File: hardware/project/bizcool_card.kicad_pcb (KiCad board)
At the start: 4 copper layers, 85.6 x 53.9 mm, 147 parts, among them J1 XL-1005SURC, J2 Conn_01x03, SW1 SW_Push, SW2 SW_Push, U1 PRTR5V0U2X, U2 ME6211C33M5G, U3 ESP32-C3FN4, U4 W25Q128JVS

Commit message: fix: LCSC component references
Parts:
- U2: value ME6211C33M5G -> AMS1117-3.3
- U4: value W25Q128JVS -> W25Q128JVSIQ
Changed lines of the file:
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@@
     (descr "Resistor SMD 0402 (1005 Metric), square (rectangular) end terminal, IPC_7351 nominal, (Body size source: IPC-SM-782 page 72, https://www.pcb-3d.com/wordpress/wp-content/uploads/ipc-sm-782a_amendment_1_and_2.pdf), generated with kicad-footprint-generator")
     (tags "resistor")
-    (property "LCSC Part" "C965790")
+    (property "LCSC Part" "C60490")
     (property "Sheetfile" "bizcool_card.kicad_sch")
     (property "Sheetname" "")
@@
     (descr "Capacitor SMD 0402 (1005 Metric), square (rectangular) end terminal, IPC_7351 nominal, (Body size source: IPC-SM-782 page 76, https://www.pcb-3d.com/wordpress/wp-content/uploads/ipc-sm-782a_amendment_1_and_2.pdf), generated with kicad-footprint-generator")
     (tags "capacitor")
+    (property "LCSC Part" "C60133")
     (property "Sheetfile" "bizcool_card.kicad_sch")
     (property "Sheetname" "")
@@
     (descr "Miniature Crystal Clock Oscillator EuroQuartz XO32 series, http://cdn-reichelt.de/documents/datenblatt/B400/XO32.pdf, 3.2x2.5mm^2 package")
     (tags "SMD SMT crystal oscillator")
-    (property "Part" "CF4040M00010001")
+    (property "LCSC Part" "C7294751")
+    (property "Part" "DF2032K76812001")
     (property "Sheetfile" "bizcool_card.kicad_sch")
     (property "Sheetname" "")
@@
     (descr "Resistor SMD 0402 (1005 Metric), square (rectangular) end terminal, IPC_7351 nominal, (Body size source: IPC-SM-782 page 72, https://www.pcb-3d.com/wordpress/wp-content/uploads/ipc-sm-782a_amendment_1_and_2.pdf), generated with kicad-footprint-generator")
     (tags "resistor")
-    (property "LCSC Part" "C965790")
+    (property "LCSC Part" "C60490")
     (property "Sheetfile" "bizcool_card.kicad_sch")
     (property "Sheetname" "")
@@
     (descr "QFN, 32 Pin (http://www.analog.com/media/en/package-pcb-resources/package/pkg_pdf/ltc-legacy-qfn/QFN_32_05-08-1693.pdf), generated with kicad-footprint-generator ipc_noLead_generator.py")
     (tags "QFN NoLead")
+    (property "LCSC Part" "C5143572")
     (property "Sheetfile" "bizcool_card.kicad_sch")
     (property "Sheetname" "")
@@
     (descr "SOIC, 8 Pin (http://www.winbond.com/resource-files/w25q32jv%20revg%2003272018%20plus.pdf#page=68), generated with kicad-footprint-generator ipc_gullwing_generator.py")
     (tags "SOIC SO")
+    (property "LCSC Part" "C97521")
     (property "Sheetfile" "bizcool_card.kicad_sch")
     (property "Sheetname" "")
@@
         (effects (font (size 1 1) (thickness 0.15)))
     )
-    (fp_text value "W25Q128JVS" (at 0 3.56) (layer "F.Fab")
+    (fp_text value "W25Q128JVSIQ" (at 0 3.56) (layer "F.Fab")
         (effects (font (size 1 1) (thickness 0.15)))
     )
@@
     (descr "Resistor SMD 0402 (1005 Metric), square (rectangular) end terminal, IPC_7351 nominal, (Body size source: IPC-SM-782 page 72, https://www.pcb-3d.com/wordpress/wp-content/uploads/ipc-sm-782a_amendment_1_and_2.pdf), generated with kicad-footprint-generator")
     (tags "resistor")
-    (property "LCSC Part" "C965790")
+    (property "LCSC Part" "C60490")
     (property "Sheetfile" "bizcool_card.kicad_sch")
     (property "Sheetname" "")
@@
     (descr "Miniature Crystal Clock Oscillator EuroQuartz XO32 series, http://cdn-reichelt.de/documents/datenblatt/B400/XO32.pdf, 3.2x2.5mm^2 package")
     (tags "SMD SMT crystal oscillator")
+    (property "LCSC Part" "C7294598")
     (property "Part" "CF4040M00010001")
     (property "Sheetfile" "bizcool_card.kicad_sch")
@@
         (effects (font (size 1 1) (thickness 0.15)))
     )
-    (fp_text value "ME6211C33M5G" (at 0 4.5 -90) (layer "F.Fab")
+    (fp_text value "AMS1117-3.3" (at 0 4.5 -90) (layer "F.Fab")
         (effects (font (size 1 1) (thickness 0.15)))
     )
@@
     (descr "Resistor SMD 0402 (1005 Metric), square (rectangular) end terminal, IPC_7351 nominal, (Body size source: IPC-SM-782 page 72, https://www.pcb-3d.com/wordpress/wp-content/uploads/ipc-sm-782a_amendment_1_and_2.pdf), generated with kicad-footprint-generator")
     (tags "resistor")
-    (property "LCSC Part" "C965790")
+    (property "LCSC Part" "C60490")
     (property "Sheetfile" "bizcool_card.kicad_sch")
     (property "Sheetname" "")
@@
   (gr_text "System Architect" (at 129.794 67.437) (layer "B.SilkS")
     (effects (font (face "Calibri") (size 4 4) (thickness 0.15)) (justify left bottom mirror))
-    (render_cache "System Architect" -0
+    (render_cache "System Architect" 0
       (polygon
         (pts
@@
   (gr_text "Check out my stuff at github.com/neta79" (at 133.055751 101.219) (layer "B.SilkS")
     (effects (font (face "Calibri") (size 3 3) (thickness 0.15)) (justify left bottom mirror))
-    (render_cache "Check out my stuff at github.com/neta79" -0
+    (render_cache "Check out my stuff at github.com/neta79" 0
       (polygon
         (pts
@@
   (gr_text "+39 3288144938\n" (at 121.79176 94.869) (layer "B.SilkS")
     (effects (font (face "OCR A Extended") (size 3.5 4) (thickness 0.15)) (justify left bottom mirror))
-    (render_cache "+39 3288144938\n" -0
+    (render_cache "+39 3288144938\n" 0
       (polygon
         (pts
@@
   (gr_text "A RISC-V gadget, with Python, Wi-Fi & Bluetooth.\n(Also, a business card)" (at 98.129513 79.756) (layer "B.SilkS")
     (effects (font (face "Calibri") (size 2.5 2.4) (thickness 0.15)) (justify bottom mirror))
-    (render_cache "A RISC-V gadget, with Python, Wi-Fi & Bluetooth.\n(Also, a business card)" -0
+    (render_cache "A RISC-V gadget, with Python, Wi-Fi & Bluetooth.\n(Also, a business card)" 0
       (polygon
         (pts
@@
   (gr_text "neta@logn.info" (at 121.79176 88.519) (layer "B.SilkS")
     (effects (font (face "OCR A Extended") (size 3.5 4) (thickness 0.15)) (justify left bottom mirror))
-    (render_cache "neta@logn.info" -0
+    (render_cache "neta@logn.info" 0
       (polygon
         (pts
@@
   (gr_text "Andrea Gronchi" (at 133.858 60.96) (layer "B.SilkS")
     (effects (font (face "Calibri") (size 6 6) (thickness 0.15)) (justify left bottom mirror))
-    (render_cache "Andrea Gronchi" -0
+    (render_cache "Andrea Gronchi" 0
       (polygon
         (pts

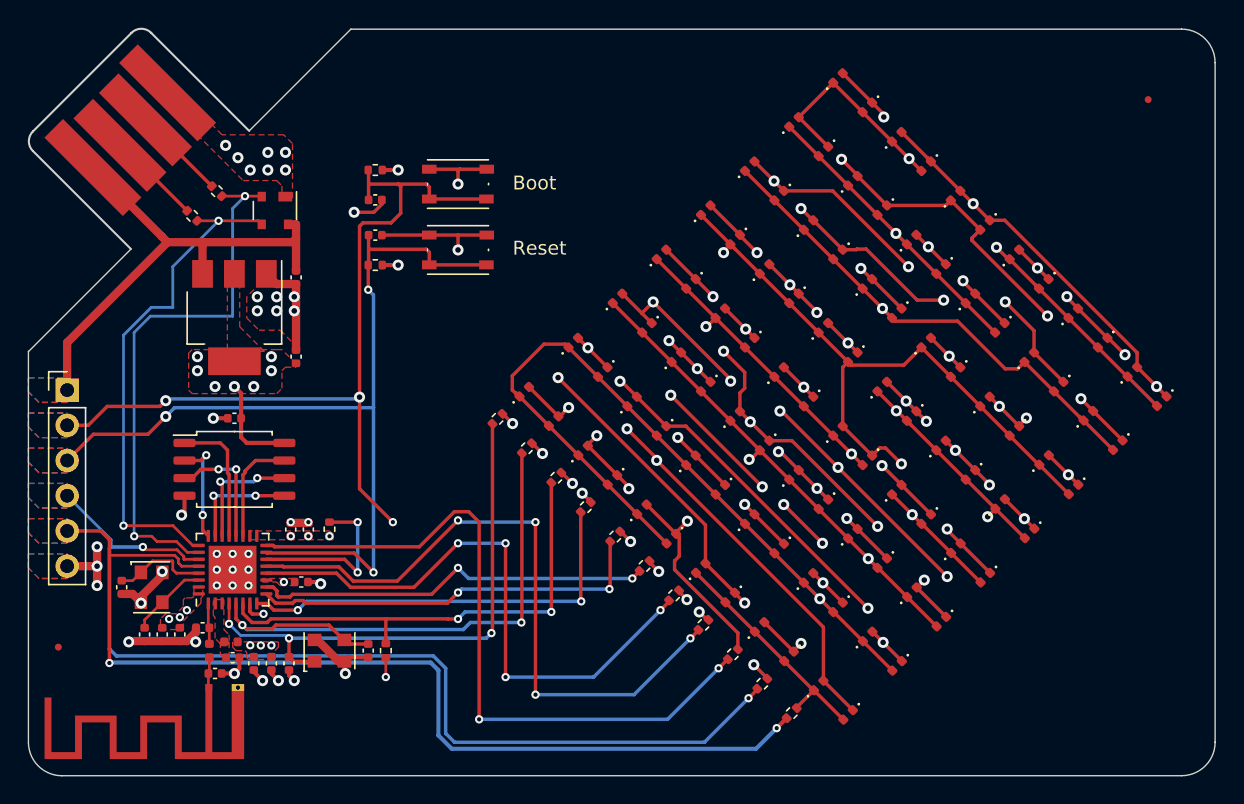
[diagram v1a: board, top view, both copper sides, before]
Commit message: fix disconnected cut outline, change push button footprints
- Edge.Cuts layer was not a properly closed shape
- adopted quite bulky 6x6 SMT push buttons (still DNP though)
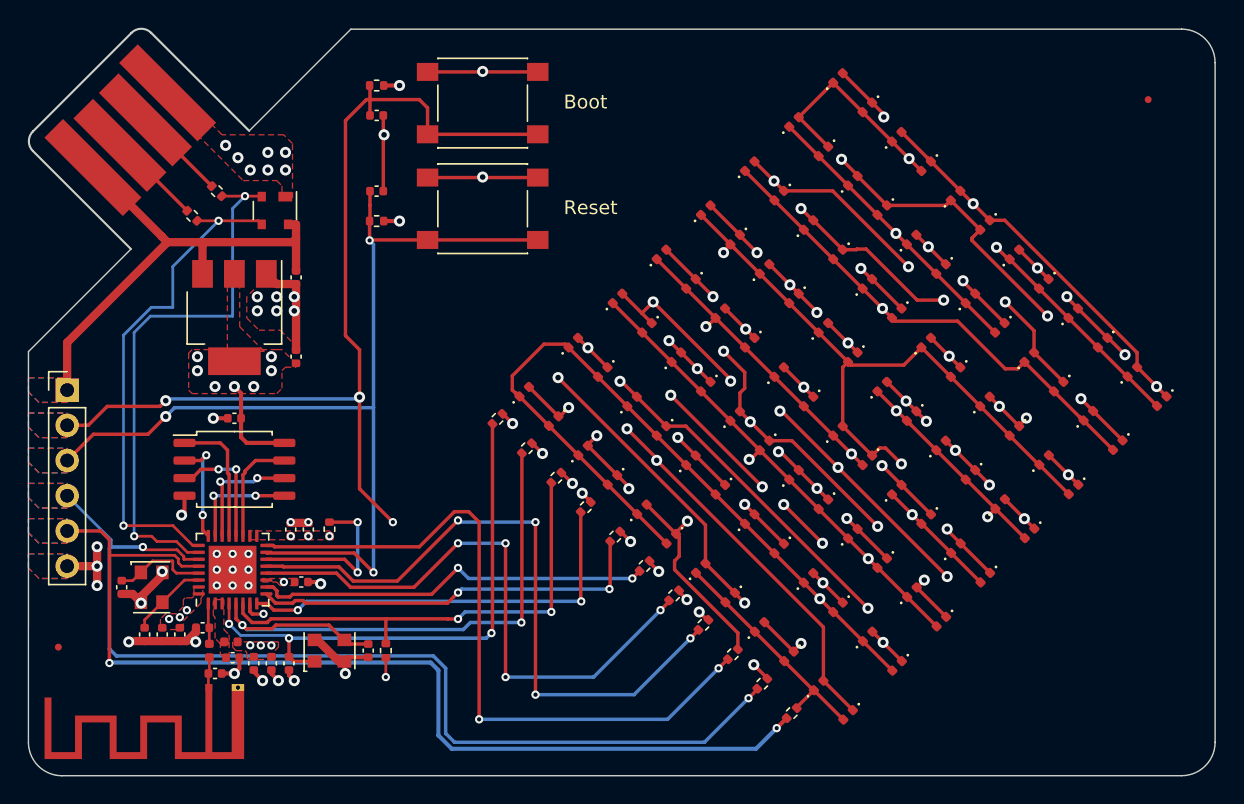
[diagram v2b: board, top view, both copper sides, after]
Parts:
- SW1, SW2: footprint Button_Switch_SMD:SW_Push_1P1T_NO_Vertical_Wuerth_434133025816 -> Button_Switch_SMD:SW_Push_1P1T_NO_6x6mm_H9.5mm
- moved SW1 6.11 mm to (83.6, 56.1)
- moved R8 6.10 mm to (75.9, 54.9)
- moved C15 6.10 mm to (75.9, 57.0)
- moved SW2 3.46 mm to (83.6, 63.8)
- moved C16 3.18 mm to (75.9, 62.5)
- moved R5 3.18 mm to (75.9, 64.6)
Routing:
- net /CHIP_RESET: track 77.3 -> 87.0 mm
- net /CHIP_BOOT: track 66.0 -> 71.8 mm
- net GND: track 54.3 -> 59.3 mm
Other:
- outline, holes or cut-outs redrawn

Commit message: fix: border connector solder mask, GND trace
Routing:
- added copper zone on B.Cu, net GND
- removed copper zone on B.Cu, net (none)
- removed copper zone on F.Cu, net (none)
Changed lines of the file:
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@@
         (effects (font (size 1 1) (thickness 0.15)))
     )
-    (fp_text value "Conn_01x03" (at 0 15.03) (layer "F.Fab")
+    (fp_text value "Conn_01x03" (at 0 15.03) (layer "F.Fab") hide
         (effects (font (size 1 1) (thickness 0.15)))
     )
-    (fp_text user "${REFERENCE}" (at 0 6.35 90) (layer "F.Fab")
+    (fp_text user "${REFERENCE}" (at 0 6.35 90) (layer "F.Fab") hide
         (effects (font (size 1 1) (thickness 0.15)))
     )
-    (fp_line (start -1.33 -1.33) (end 0 -1.33)
-      (stroke (width 0.12) (type solid)) (layer "F.SilkS"))
-    (fp_line (start -1.33 0) (end -1.33 -1.33)
-      (stroke (width 0.12) (type solid)) (layer "F.SilkS"))
-    (fp_line (start -1.33 1.27) (end -1.33 14.03)
-      (stroke (width 0.12) (type solid)) (layer "F.SilkS"))
-    (fp_line (start -1.33 1.27) (end 1.33 1.27)
-      (stroke (width 0.12) (type solid)) (layer "F.SilkS"))
-    (fp_line (start -1.33 14.03) (end 1.33 14.03)
-      (stroke (width 0.12) (type solid)) (layer "F.SilkS"))
-    (fp_line (start 1.33 1.27) (end 1.33 14.03)
-      (stroke (width 0.12) (type solid)) (layer "F.SilkS"))
     (fp_line (start -1.8 -1.8) (end -1.8 14.5)
       (stroke (width 0.05) (type solid)) (layer "F.CrtYd"))
@@
     )
   )
+  (gr_poly
+    (pts
+      (xy 53.65 90.4)
+      (xy 51.6 90.4)
+      (xy 50.85 89.65)
+      (xy 50.85 88.65)
+      (xy 53.65 88.65)
+    )
+    (stroke (width 0.15) (type solid)) (fill solid) (layer "B.Mask"))
+  (gr_poly
+    (pts
+      (xy 53.65 87.85)
+      (xy 51.6 87.85)
+      (xy 50.85 87.1)
+      (xy 50.85 86.1)
+      (xy 53.65 86.1)
+    )
+    (stroke (width 0.15) (type solid)) (fill solid) (layer "B.Mask"))
+  (gr_poly
+    (pts
+      (xy 53.65 77.7)
+      (xy 51.6 77.7)
+      (xy 50.85 76.95)
+      (xy 50.85 75.95)
+      (xy 53.65 75.95)
+    )
+    (stroke (width 0.15) (type solid)) (fill solid) (layer "B.Mask"))
+  (gr_poly
+    (pts
+      (xy 53.65 82.8)
+      (xy 51.6 82.8)
+      (xy 50.85 82.05)
+      (xy 50.85 81.05)
+      (xy 53.65 81.05)
+    )
+    (stroke (width 0.15) (type solid)) (fill solid) (layer "B.Mask"))
+  (gr_poly
+    (pts
+      (xy 53.65 80.25)
+      (xy 51.6 80.25)
+      (xy 50.85 79.5)
+      (xy 50.85 78.5)
+      (xy 53.65 78.5)
+    )
+    (stroke (width 0.15) (type solid)) (fill solid) (layer "B.Mask"))
+  (gr_poly
+    (pts
+      (xy 53.65 85.35)
+      (xy 51.6 85.35)
+      (xy 50.85 84.6)
+      (xy 50.85 83.6)
+      (xy 53.65 83.6)
+    )
+    (stroke (width 0.15) (type solid)) (fill solid) (layer "B.Mask"))
+  (gr_poly
+    (pts
+      (xy 53.6 90.4)
+      (xy 51.55 90.4)
+      (xy 50.8 89.65)
+      (xy 50.8 88.65)
+      (xy 53.6 88.65)
+    )
+    (stroke (width 0.15) (type solid)) (fill solid) (layer "F.Mask"))
+  (gr_poly
+    (pts
+      (xy 53.65 85.3)
+      (xy 51.6 85.3)
+      (xy 50.85 84.55)
+      (xy 50.85 83.55)
+      (xy 53.65 83.55)
+    )
+    (stroke (width 0.15) (type solid)) (fill solid) (layer "F.Mask"))
+  (gr_poly
+    (pts
+      (xy 53.65 80.25)
+      (xy 51.6 80.25)
+      (xy 50.85 79.5)
+      (xy 50.85 78.5)
+      (xy 53.65 78.5)
+    )
+    (stroke (width 0.15) (type solid)) (fill solid) (layer "F.Mask"))
+  (gr_poly
+    (pts
+      (xy 53.65 87.9)
+      (xy 51.6 87.9)
+      (xy 50.85 87.15)
+      (xy 50.85 86.15)
+      (xy 53.65 86.15)
+    )
+    (stroke (width 0.15) (type solid)) (fill solid) (layer "F.Mask"))
+  (gr_poly
+    (pts
+      (xy 53.65 77.7)
+      (xy 51.6 77.7)
+      (xy 50.85 76.95)
+      (xy 50.85 75.95)
+      (xy 53.65 75.95)
+    )
+    (stroke (width 0.15) (type solid)) (fill solid) (layer "F.Mask"))
+  (gr_poly
+    (pts
+      (xy 53.65 82.8)
+      (xy 51.6 82.8)
+      (xy 50.85 82.05)
+      (xy 50.85 81.05)
+      (xy 53.65 81.05)
+    )
+    (stroke (width 0.15) (type solid)) (fill solid) (layer "F.Mask"))
   (gr_line (start 50.8 102.235) (end 50.804853 74.054297)
     (stroke (width 0.1) (type default)) (layer "Edge.Cuts"))
@@
     )
   )
-  (zone (net 0) (net_name "") (layers "F&B.Cu") (hatch edge 0.5)
+  (zone (net 2) (net_name "GND") (layers "F&B.Cu") (hatch edge 0.5)
     (priority 12)
     (connect_pads yes (clearance 0.2))

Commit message: change LDO regulator
switched to a SOT-23-3 LDO reg, a smaller one (400mA).
technically not in-spec, should use 2 of these.
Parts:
- U2: value AMS1117-3.3 -> H7233-1; footprint Package_TO_SOT_SMD:SOT-223-3_TabPin2 -> Package_TO_SOT_SMD:SOT-23-3
- moved C6 8.73 mm to (62.2, 70.6)
- moved C5 2.64 mm to (67.5, 68.0), turned to 180 degrees
- moved U2 1.06 mm to (66.0, 70.6), turned to 0 degrees
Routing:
- net /VUSB: track 36.9 -> 32.3 mm
- net GND: track 59.3 -> 55.2 mm, vias 42 -> 40
- net /VDD3_3: track 12.6 -> 16.6 mm, vias 20 -> 17
- net /USB_DP: track 39.4 -> 35.9 mm
- net /USB_DN: track 36.5 -> 35.6 mm

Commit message: design sent for a test print
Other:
- board text added: "+39 328 8144938"
- board text added: "Runs your Python code. Has Wi-Fi, Bluetooth & pretty lights. (Also, it's a business card)"
- board text added: "Software Architect - Consultant"
- board text added: "This RISC-V-powered gadget:"
- board text added: "{"
- board text added: "}"
- board text removed: "+39 3288144938"
- board text removed: "A RISC-V gadget, with Python, Wi-Fi & Bluetooth. (Also, a business card)"
- board text removed: "System Architect"

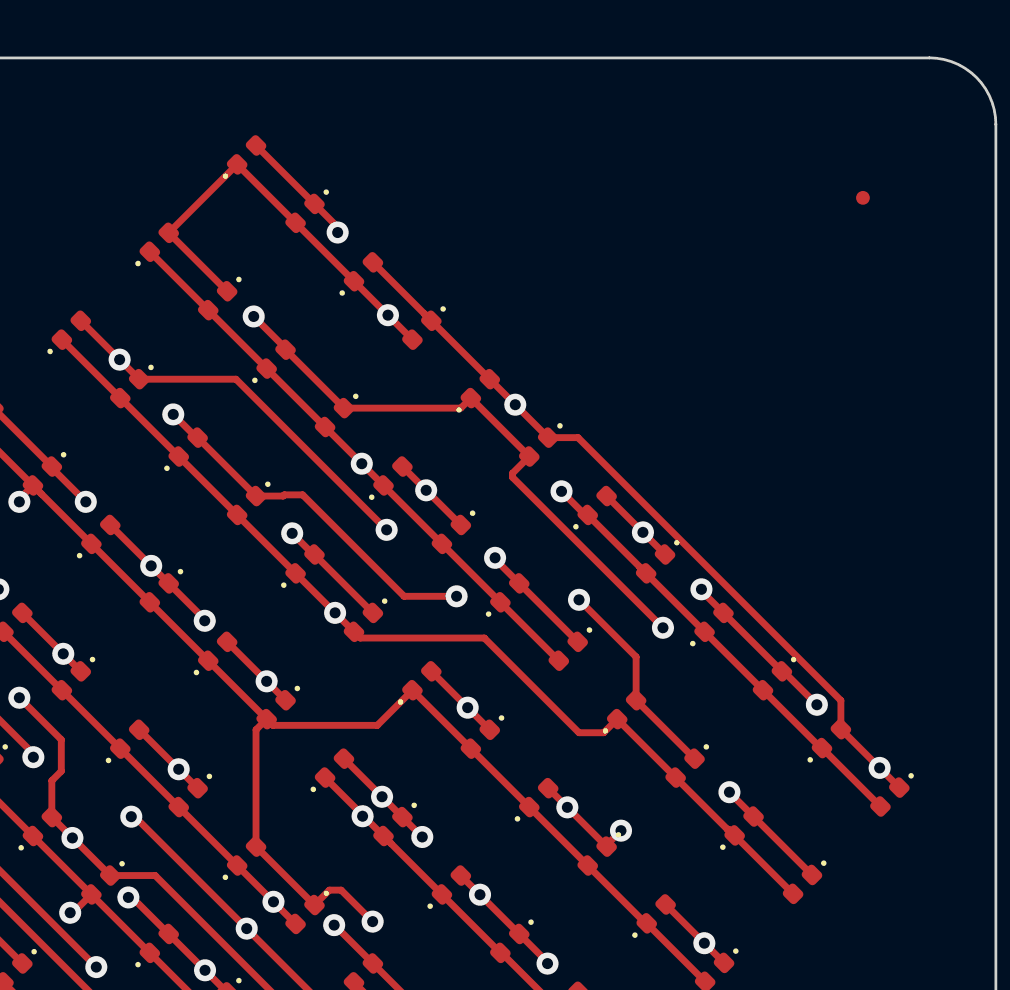
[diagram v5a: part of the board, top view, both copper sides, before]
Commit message: fix: d1-d6 reordering, re-routing
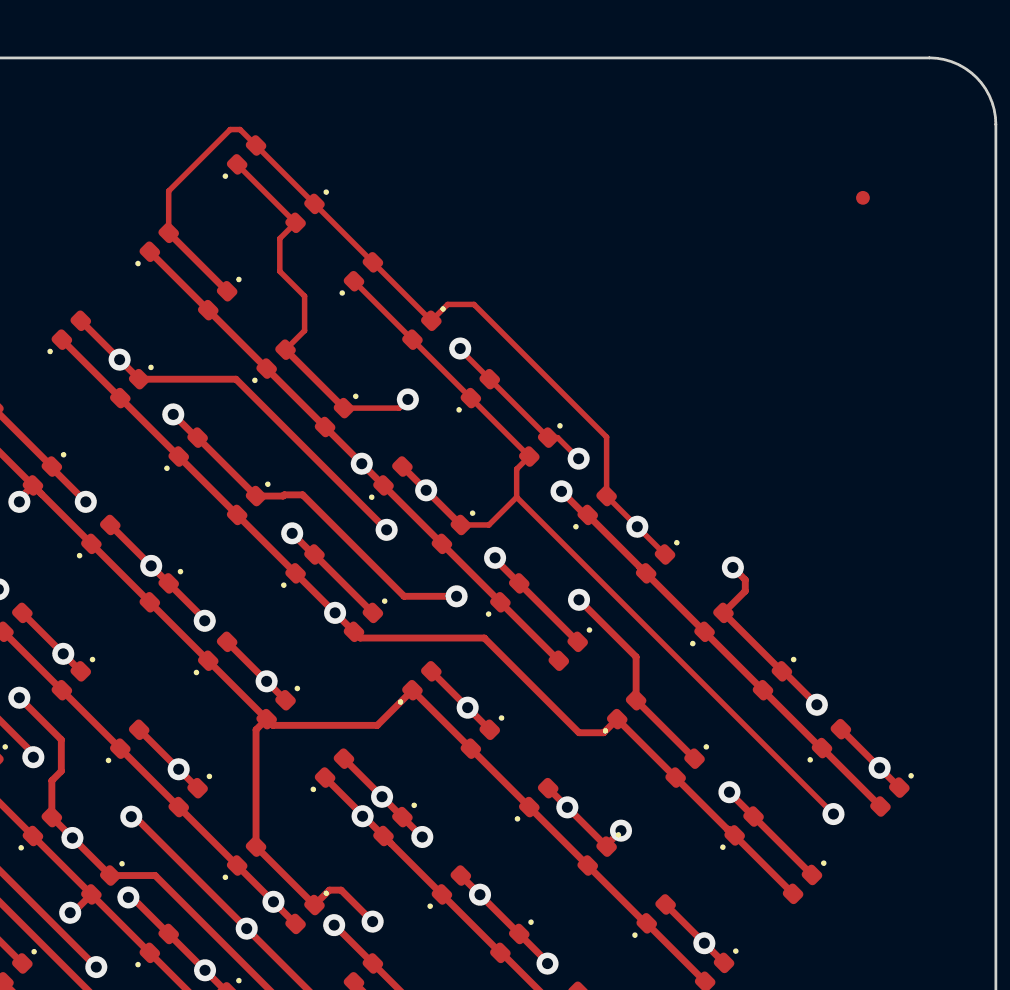
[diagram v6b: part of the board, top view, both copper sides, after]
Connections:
- D10 pad 1: Net-(D1-A) -> Net-(D1-K)
- D13 pad 2: Net-(D1-K) -> Net-(D1-A)
- D14 pad 1: Net-(D1-K) -> Net-(D1-A)
- D15 pad 2: Net-(D1-A) -> Net-(D1-K)
- D16 pad 1: Net-(D1-A) -> Net-(D1-K)
- D21 pad 2: Net-(D1-K) -> Net-(D1-A)
- D22 pad 1: Net-(D1-K) -> Net-(D1-A)
- D23 pad 2: Net-(D1-A) -> Net-(D1-K)
- D24 pad 1: Net-(D1-A) -> Net-(D1-K)
- D3 pad 1: Net-(D1-K) -> Net-(D11-A)
- D3 pad 2: Net-(D11-A) -> Net-(D1-A)
- D31 pad 2: Net-(D1-K) -> Net-(D1-A)
- D32 pad 1: Net-(D1-K) -> Net-(D1-A)
- D33 pad 2: Net-(D1-A) -> Net-(D1-K)
- D34 pad 1: Net-(D1-A) -> Net-(D1-K)
- D4 pad 1: Net-(D11-A) -> Net-(D1-A)
- D4 pad 2: Net-(D1-K) -> Net-(D11-A)
- D43 pad 2: Net-(D1-K) -> Net-(D1-A)
- D44 pad 1: Net-(D1-K) -> Net-(D1-A)
- D45 pad 2: Net-(D1-A) -> Net-(D1-K)
- D46 pad 1: Net-(D1-A) -> Net-(D1-K)
- D5 pad 1: Net-(D1-A) -> Net-(D11-A)
- D5 pad 2: Net-(D11-A) -> Net-(D1-K)
- D57 pad 2: Net-(D1-K) -> Net-(D1-A)
- D58 pad 1: Net-(D1-K) -> Net-(D1-A)
- D59 pad 2: Net-(D1-A) -> Net-(D1-K)
- D6 pad 1: Net-(D11-A) -> Net-(D1-K)
- D6 pad 2: Net-(D1-A) -> Net-(D11-A)
- D60 pad 1: Net-(D1-A) -> Net-(D1-K)
- D7 pad 2: Net-(D1-K) -> Net-(D1-A)
- D73 pad 2: Net-(D1-K) -> Net-(D1-A)
- D74 pad 1: Net-(D1-K) -> Net-(D1-A)
- D75 pad 2: Net-(D1-A) -> Net-(D1-K)
- D76 pad 1: Net-(D1-A) -> Net-(D1-K)
- D8 pad 1: Net-(D1-K) -> Net-(D1-A)
- D9 pad 2: Net-(D1-A) -> Net-(D1-K)
- D91 pad 2: Net-(D1-K) -> Net-(D1-A)
- D92 pad 1: Net-(D1-K) -> Net-(D1-A)
- D93 pad 2: Net-(D1-A) -> Net-(D1-K)
- D94 pad 1: Net-(D1-A) -> Net-(D1-K)
- R10 pad 2: Net-(D1-A) -> Net-(D1-K)
- R9 pad 2: Net-(D1-K) -> Net-(D1-A)
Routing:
- net Net-(D1-A): track 124.0 -> 116.9 mm, vias 15 -> 10
- net Net-(D1-K): track 118.5 -> 123.0 mm, vias 11 -> 15
